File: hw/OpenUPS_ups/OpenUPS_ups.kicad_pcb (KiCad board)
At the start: 4 copper layers, 90 x 62 mm, 283 parts, among them J1001 USB4105-GF-A, J101 Barrel Jack, J102 XT30PW-M, J103 XT30PW-M, J104 S2B-PH-K_1x02, J105 S2B-PH-K_1x02, J106 Screw Terminal, J107 Screw Terminal, J108 Screw Terminal, J109 JST XH, J110 JST XH, J501 Conn_01x03, J701 0022053031, J702 0022053031, J901 Qwiic, J902 Qwiic, Q1001 2N7002, Q301 AON7534, Q302 AON7534, Q303 AON7534, Q304 AON7534, Q401 2N7002, Q402 AON7534, Q403 AON7534, Q404 AON7534, Q405 AON7534, Q601 AON7534, Q602 AON7534, Q603 AON7534, Q604 AON7534, Q701 2N7002, Q702 2N7002, U1001 MCP6547, U1002 AP22814BW5, U1003 NUP2301MW6T1G, U101 AVR32DB48x-xPT, U102 NUP2301MW6T1G, U103 LM75BTP,147, U201 TPS51397A, U202 INA180A3, U301 NCP81599, U401 NCP431, U402 BD99950, U403 MCP6001R, U404 DZDH0401DW, U405 INA180A1, U601 NCP81599, U701 NUP2301MW6T1G, U702 NUP2301MW6T1G, U801 AP7383-33W5, U901 π220N31

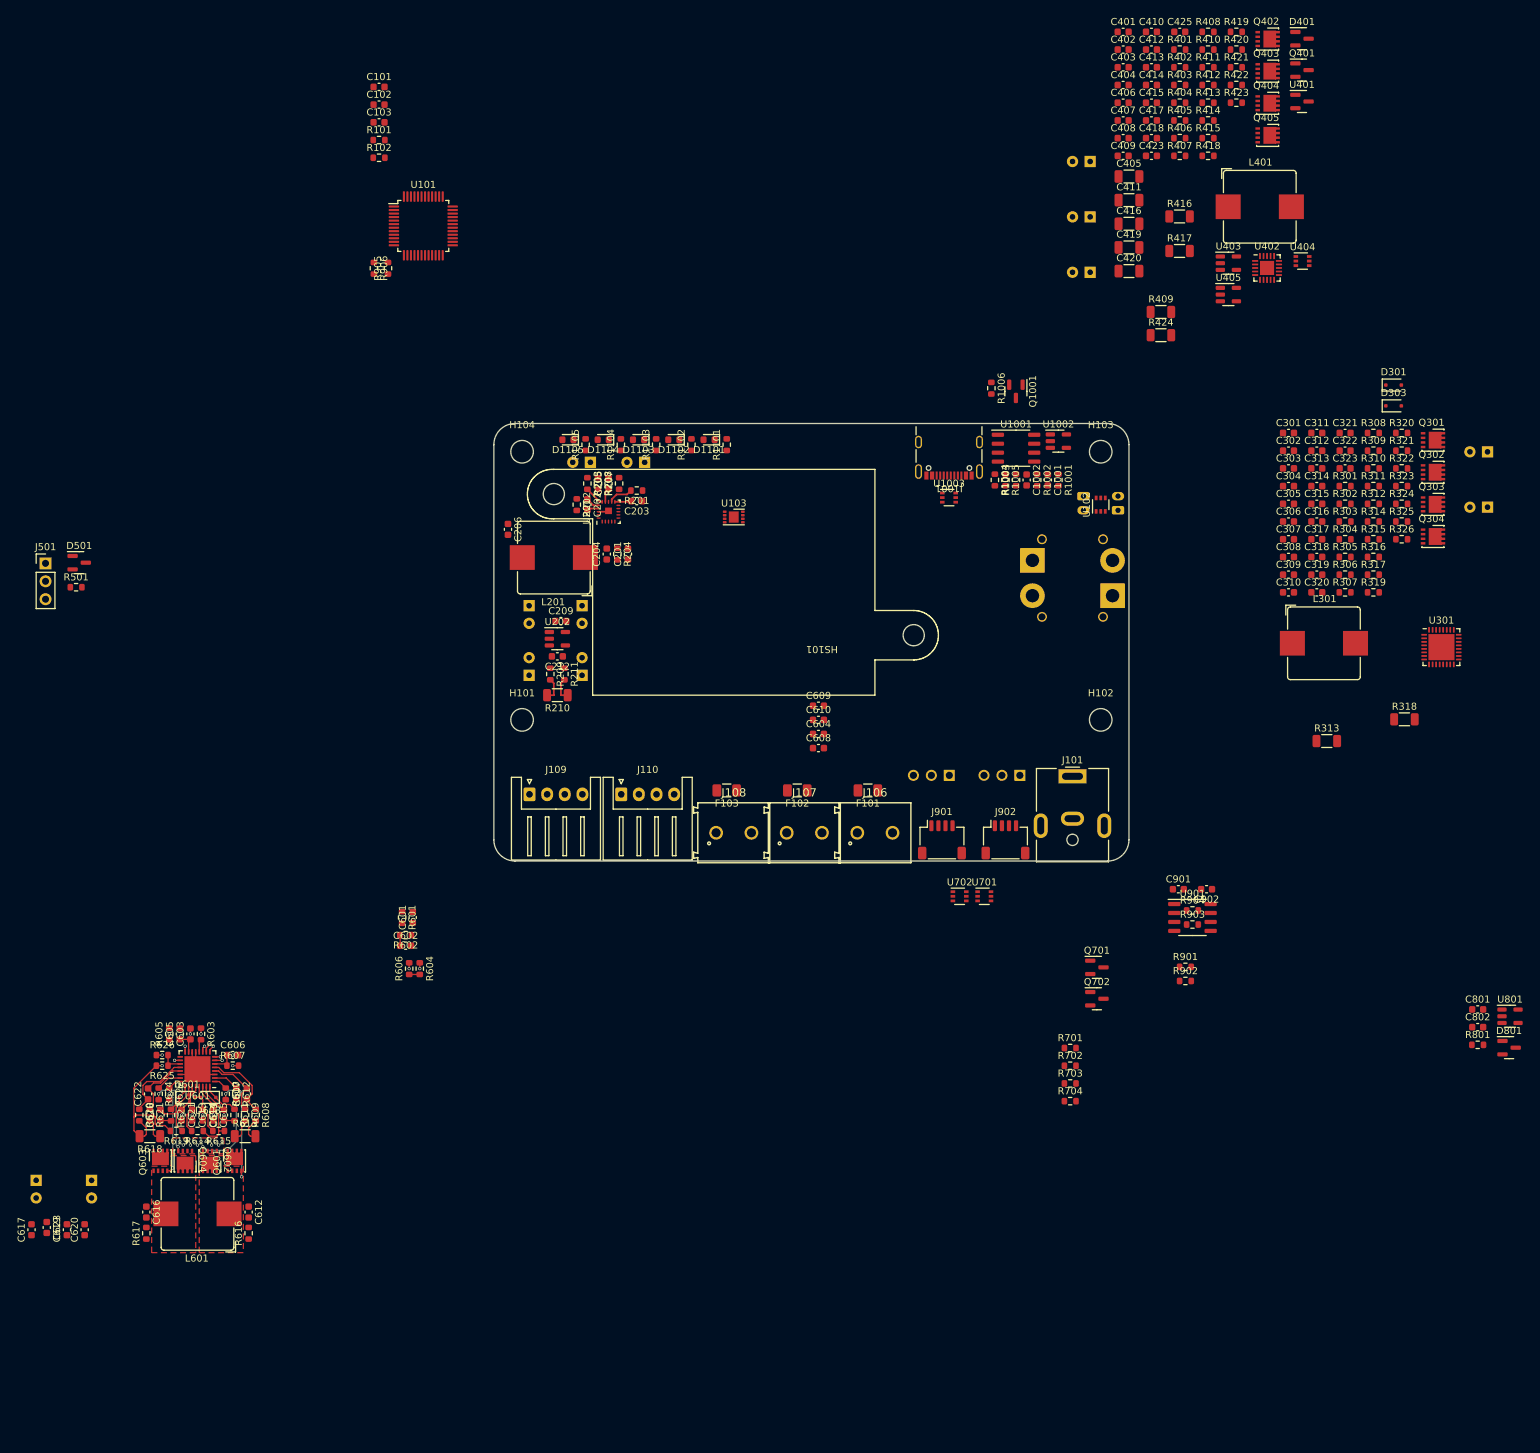
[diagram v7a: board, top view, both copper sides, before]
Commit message: Converter placement
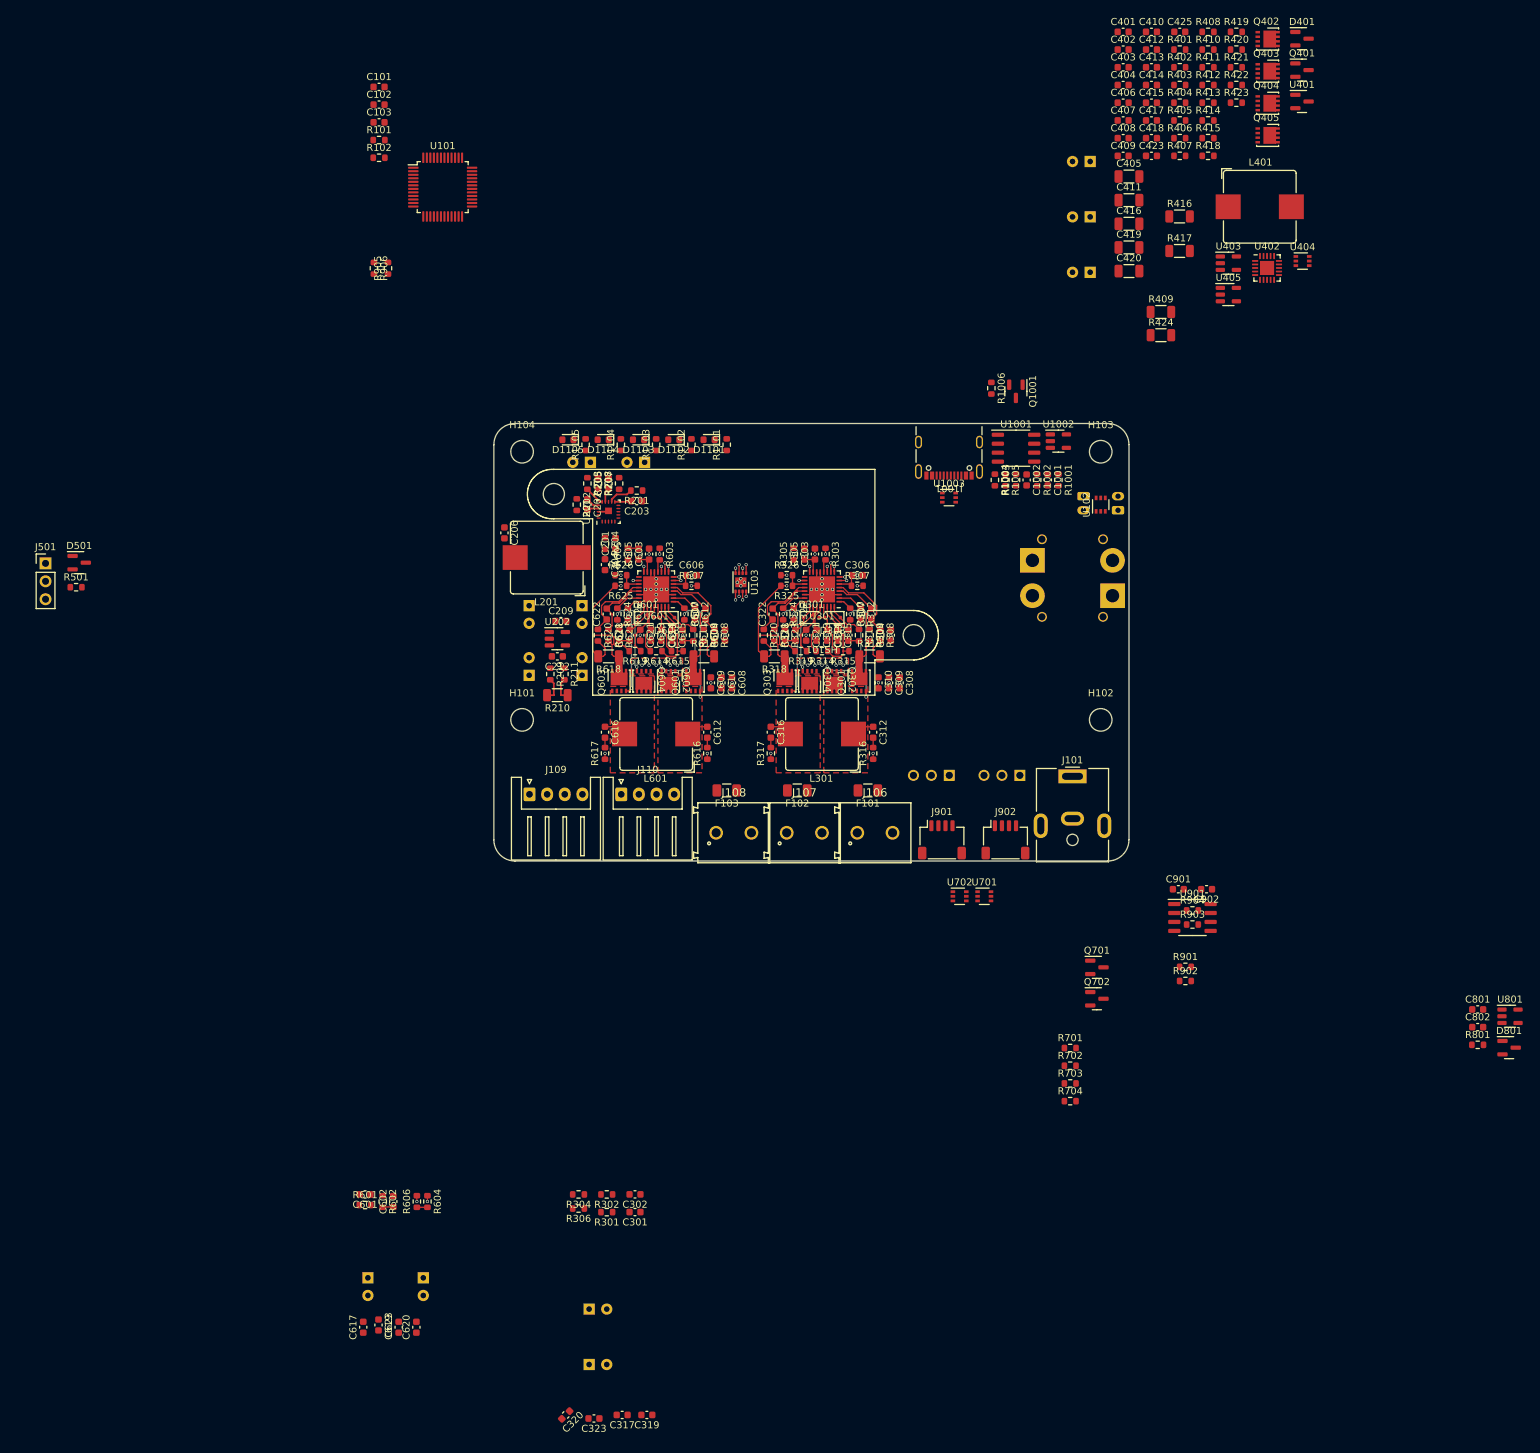
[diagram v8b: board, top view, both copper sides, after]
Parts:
- moved C324 181.5 mm to (96.5, 205.3), turned to 0 degrees
- moved C323 171.6 mm to (97.2, 213.0), turned to 180 degrees
- moved C325 170.7 mm to (96.5, 197.5), turned to 0 degrees
- moved C317 158.4 mm to (101.2, 212.5), turned to 180 degrees
- moved C320 157.9 mm to (93.2, 212.5), turned to -135 degrees
- moved C319 152.3 mm to (104.7, 212.5), turned to 180 degrees
- moved R301 146.7 mm to (99.0, 183.8), turned to 180 degrees
- moved C301 144.1 mm to (103.0, 183.8), turned to 180 degrees
- moved R302 143.3 mm to (99.0, 181.2), turned to 180 degrees
- moved R304 142.9 mm to (95.0, 181.2), turned to 180 degrees
- moved R306 141.0 mm to (95.0, 183.2), turned to 180 degrees
- moved C302 140.3 mm to (103.0, 181.2), turned to 180 degrees
- moved Q303 95.2 mm to (124.2, 108.5), turned to 90 degrees
- moved C618 95.1 mm to (102.2, 102.0)
- moved R320 94.8 mm to (121.2, 102.0), turned to -90 degrees
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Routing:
- net GND: track 22.1 -> 53.4 mm, vias 10 -> 81
- net +AdjV: track 0.00 -> 22.7 mm, vias 0 -> 1
- net Net-(Q301-G): track 0.00 -> 16.2 mm, vias 0 -> 2
- net Net-(Q302-G): track 0.00 -> 13.7 mm, vias 0 -> 2
- net Net-(Q303-G): track 0.00 -> 12.5 mm, vias 0 -> 2
- net Net-(Q304-G): track 0.00 -> 12.1 mm, vias 0 -> 2
- net Net-(U301A-VCC): track 0.00 -> 11.1 mm
- net Net-(U301B-CSP1): track 0.00 -> 10.6 mm
- net Net-(U301C-CSN2): track 0.00 -> 10.5 mm
- net Net-(U301C-CSP2): track 0.00 -> 9.04 mm
- net Net-(U301B-CSN1): track 0.00 -> 9.03 mm
- net Net-(U301B-VSW1): track 0.00 -> 8.41 mm, vias 0 -> 1
- net Net-(U301C-VSW2): track 0.00 -> 7.96 mm
- net /Adj_Buck_Boost/VDRV: track 0.00 -> 7.90 mm
- net Net-(U301C-V2): track 0.00 -> 7.56 mm
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- added copper zone on F.Cu, net Net-(U301B-VSW1)
- added copper zone on F.Cu, net Net-(U301C-VSW2)
